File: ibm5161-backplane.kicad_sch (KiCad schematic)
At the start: 33 parts, among them J1 Bus_ISA_8bit, J2 Bus_ISA_8bit, J3 Bus_ISA_8bit, J4 Bus_ISA_8bit, J5 Bus_ISA_8bit, J6 Bus_ISA_8bit, J7 Bus_ISA_8bit, J8 Bus_ISA_8bit, P1 Molex 15-48-0106, P2 Molex 15-48-0106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

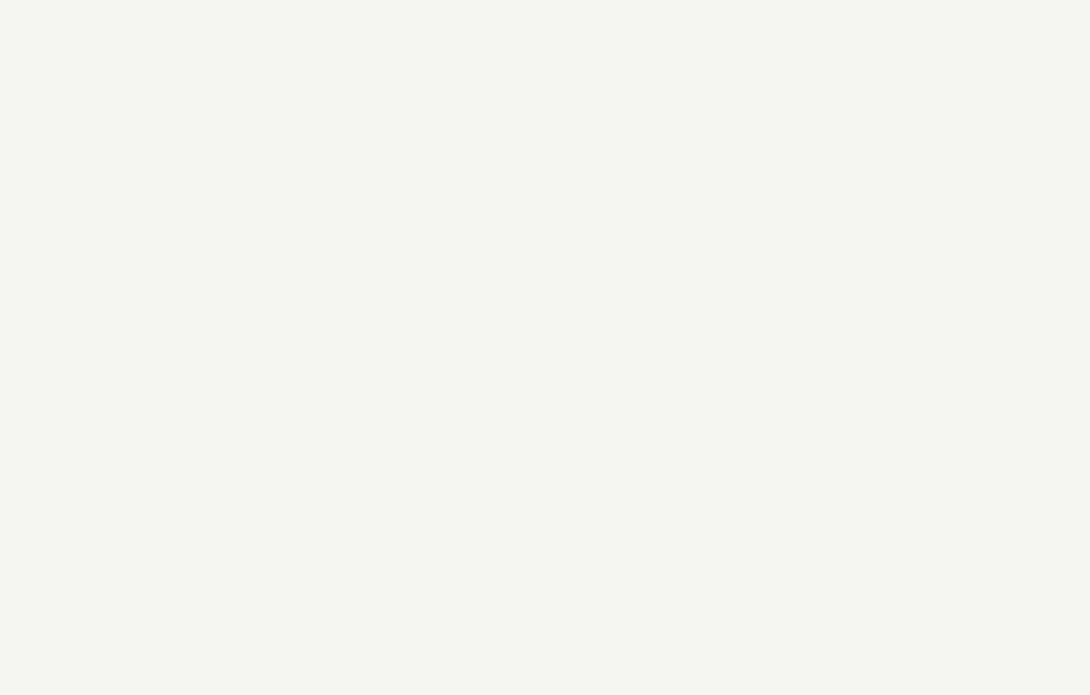
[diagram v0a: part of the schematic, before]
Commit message: Added 24 pin ATX connector and negative voltage regulator to schematic.
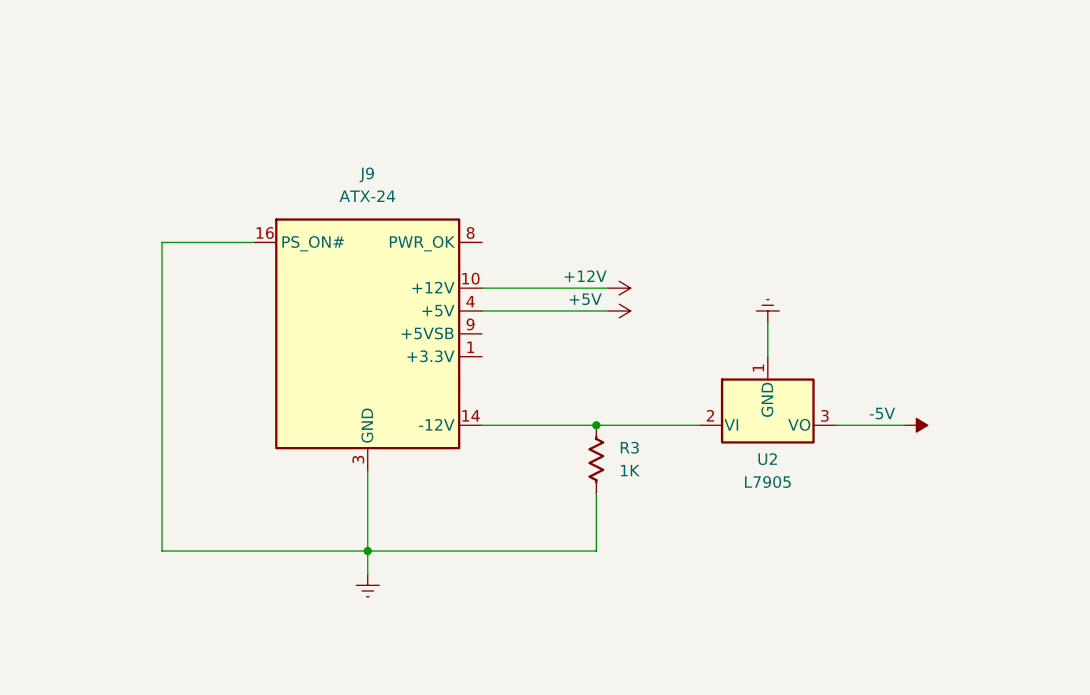
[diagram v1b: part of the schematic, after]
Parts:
- added J9: ATX-24, SamacSys_Parts:1-1775099-3, symbol Connector:ATX-24
- added R3: 1K, Library:R_Axial_DIN0207_L6.3mm_D2.5mm_P12.70mm_Horizontal, symbol Resistor_US_AKL:R_DIN0207_P10.16mm
- added U2: L7905, SamacSys_Parts:TO270P460X1020X2008-3P, symbol Regulator_Linear:L7905
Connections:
- net +12V: now also J9.10 (+12V), J9.11 (+12V)
- net +5V: now also J9.21 (+5V), J9.22 (+5V), J9.23 (+5V), J9.4 (+5V), J9.6 (+5V)
- net -5V: now also U2.3 (VO)
- net GNDREF: now also J9.15 (GND), J9.16 (PS_ON#), J9.17 (GND), J9.18 (GND), J9.19 (GND), J9.24 (GND), J9.3 (GND), J9.5 (GND), J9.7 (GND), R3.2, U2.1 (GND)
- new net: J9.1 (+3.3V), J9.12 (+3.3V), J9.13 (+3.3V), J9.2 (+3.3V)
- new net: J9.14 (-12V), R3.1, U2.2 (VI)

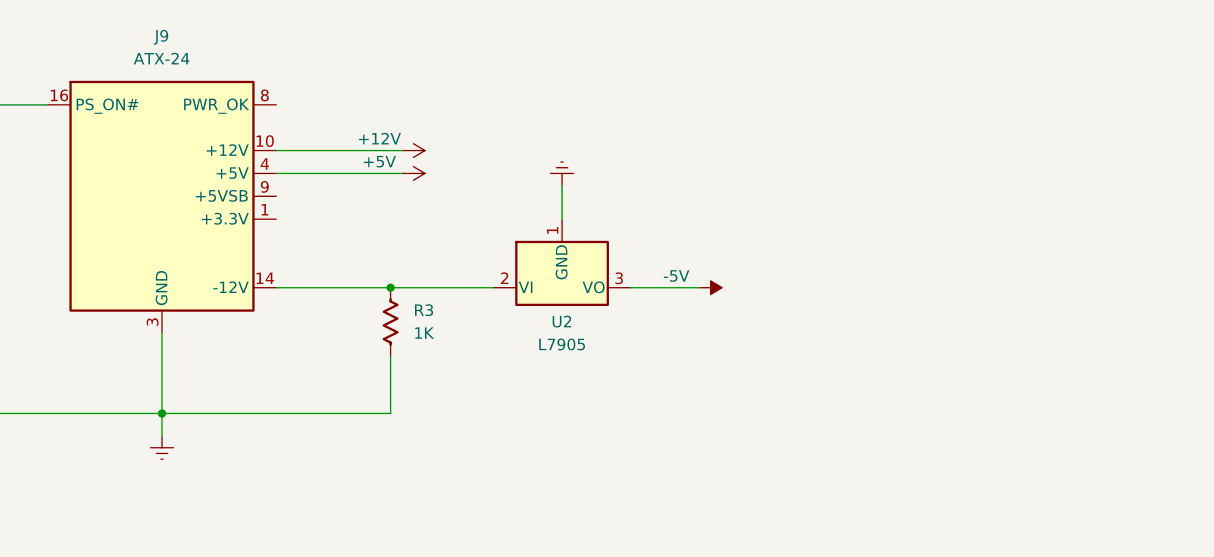
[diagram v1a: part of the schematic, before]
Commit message: Added filter caps for the L7905 and a dummy load resistor for its output
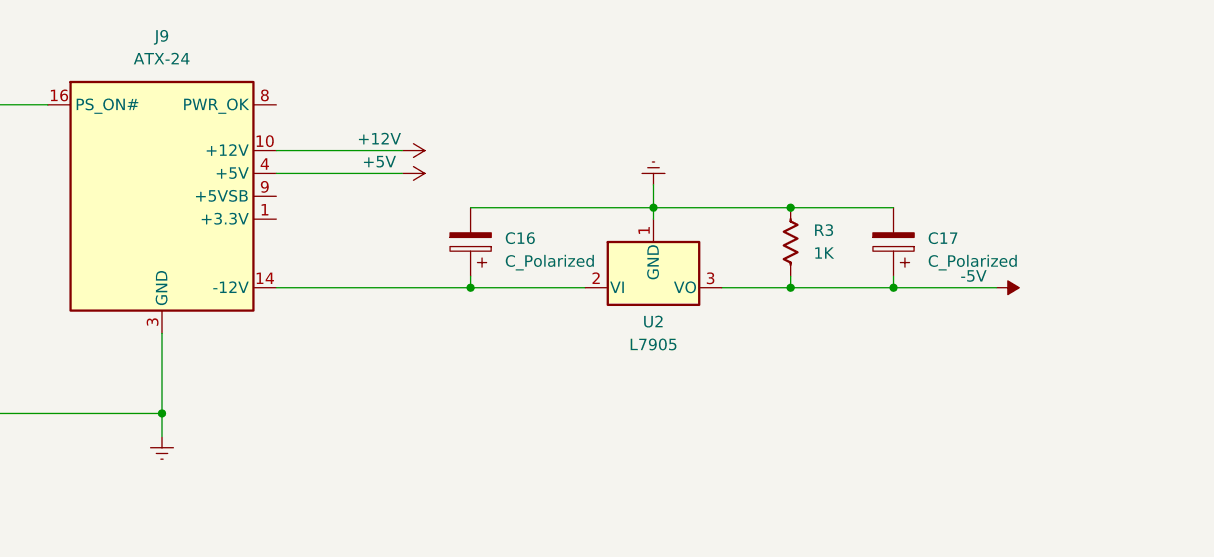
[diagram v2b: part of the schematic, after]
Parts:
- added C16, C17: C_Polarized, symbol Device:C_Polarized
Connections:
- net -5V: now also R3.2, C17.1
- net GNDREF: now also R3.1, C16.2, C17.2; no longer R3.2
- net at J9.14 (-12V), U2.2 (VI): now also C16.1; no longer R3.1
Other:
- moved on the sheet: U2

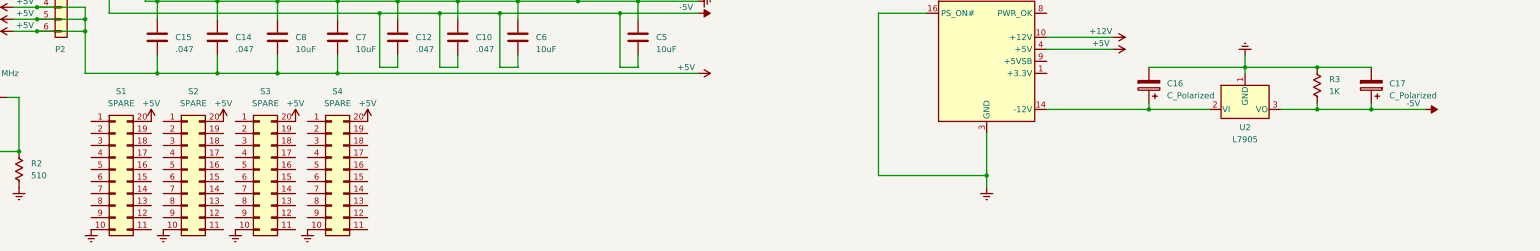
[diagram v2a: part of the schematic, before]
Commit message: Removed spare slots. Schematic cleanup.
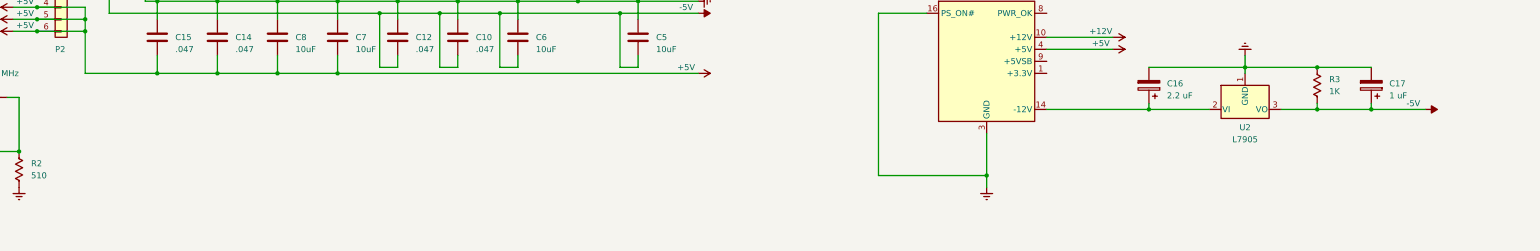
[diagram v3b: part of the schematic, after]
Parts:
- removed S1, S2, S3, S4: SPARE, Library:DIP-20_W7.62mm_Socket SQ, symbol Connector_Generic:Conn_02x10_Counter_Clockwise
- C16: value C_Polarized -> 2.2 uF; footprint (none) -> Capacitor_THT:CP_Radial_D5.0mm_P2.50mm
- C17: value C_Polarized -> 1 uF; footprint (none) -> Capacitor_THT:CP_Radial_D5.0mm_P2.50mm

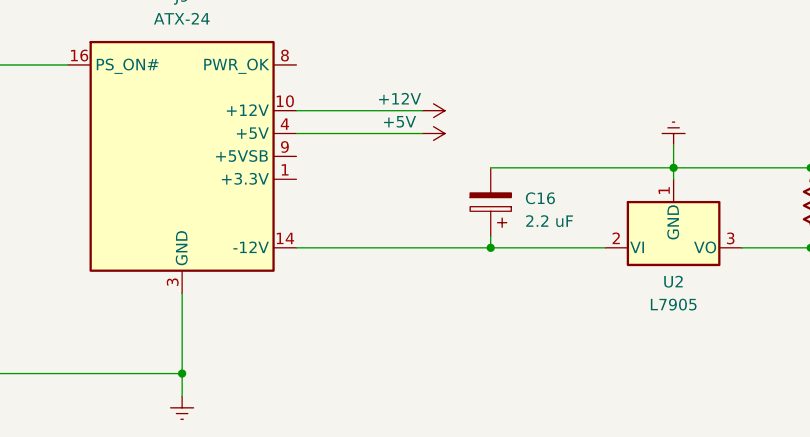
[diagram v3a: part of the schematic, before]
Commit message: Connected -12V from 24 pin to -12V rail.
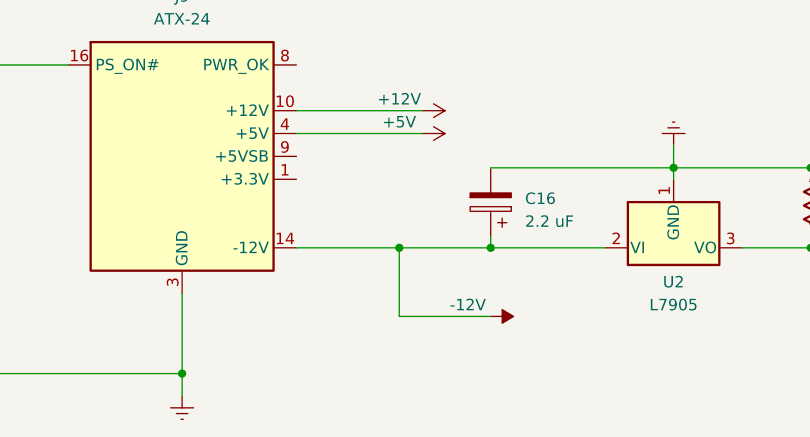
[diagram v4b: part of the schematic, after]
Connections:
- net -12V: now also C16.1, J9.14 (-12V), U2.2 (VI)
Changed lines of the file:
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@@
 	)
 	(junction
+		(at 320.04 168.91)
+		(diameter 0)
+		(color 0 0 0 0)
+	)
+	(junction
 		(at 158.75 161.29)
 		(diameter 0)
@@
 	(wire
 		(pts
+			(xy 320.04 168.91) (xy 320.04 176.53)
+		)
+		(stroke
+			(width 0)
+			(type default)
+		)
+	)
+	(wire
+		(pts
 			(xy 377.19 88.9) (xy 386.08 88.9)
 		)
@@
 	(wire
 		(pts
-			(xy 308.61 168.91) (xy 330.2 168.91)
+			(xy 308.61 168.91) (xy 320.04 168.91)
 		)
 		(stroke
@@
 		)
 	)
+	(wire
+		(pts
+			(xy 320.04 168.91) (xy 330.2 168.91)
+		)
+		(stroke
+			(width 0)
+			(type default)
+		)
+	)
 	(bus
 		(pts
@@
 	(wire
 		(pts
+			(xy 320.04 176.53) (xy 330.2 176.53)
+		)
+		(stroke
+			(width 0)
+			(type default)
+		)
+	)
+	(wire
+		(pts
 			(xy 184.15 146.05) (xy 171.45 146.05)
 		)
@@
 					(unit 1)
 				)
+			)
+		)
+	)
+	(symbol
+		(lib_id "power:-12V")
+		(at 330.2 176.53 270)
+		(mirror x)
+		(unit 1)
+		(exclude_from_sim no)
+		(in_bom yes)
+		(on_board yes)
+		(dnp no)
+		(property "Reference" "#PWR088"
+			(at 332.74 176.53 0)
+			(effects
+				(font
+					(size 1.27 1.27)
+				)
+				(hide yes)
+			)
+		)
+		(property "Value" "-12V"
+			(at 327.66 175.26 90)
+			(effects
+				(font
+					(size 1.27 1.27)
+				)
+			)
+		)
+		(property "Footprint" ""
+			(at 330.2 176.53 0)
+			(effects
+				(font
+					(size 1.27 1.27)
+				)
+				(hide yes)
+			)
+		)
+		(property "Datasheet" ""
+			(at 330.2 176.53 0)
+			(effects
+				(font
+					(size 1.27 1.27)
+				)
+				(hide yes)
+			)
+		)
+		(property "Description" ""
+			(at 330.2 176.53 0)
+			(effects
+				(font
+					(size 1.27 1.27)
+				)
+				(hide yes)
+			)
+		)
+		(pin "1"
+		)
+		(instances
+			(project "ibm5161-backplane"
+				(path "/3153ab07-b19d-413d-9c02-432affa22f92"
+					(reference "#PWR088")
+					(unit 1)
+				)

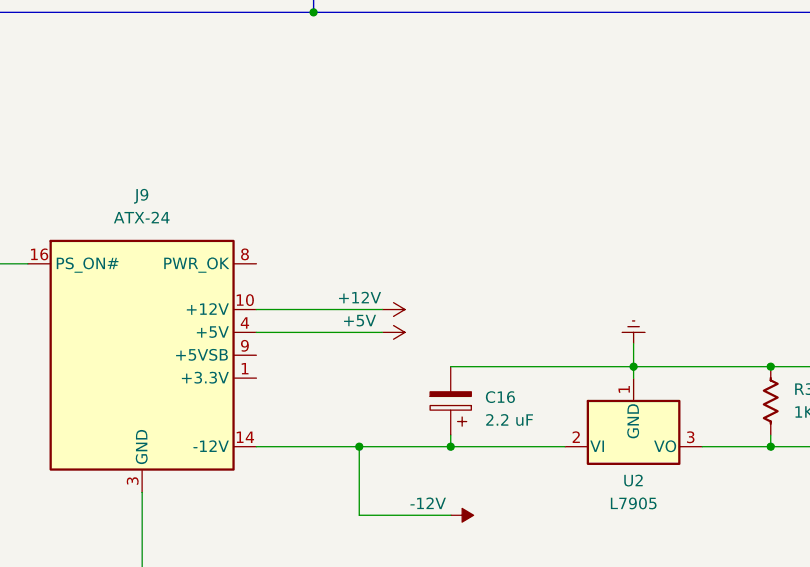
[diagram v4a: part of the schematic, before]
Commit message: Flipped 24 pin connector for easier routing. Added PWR Good LED.
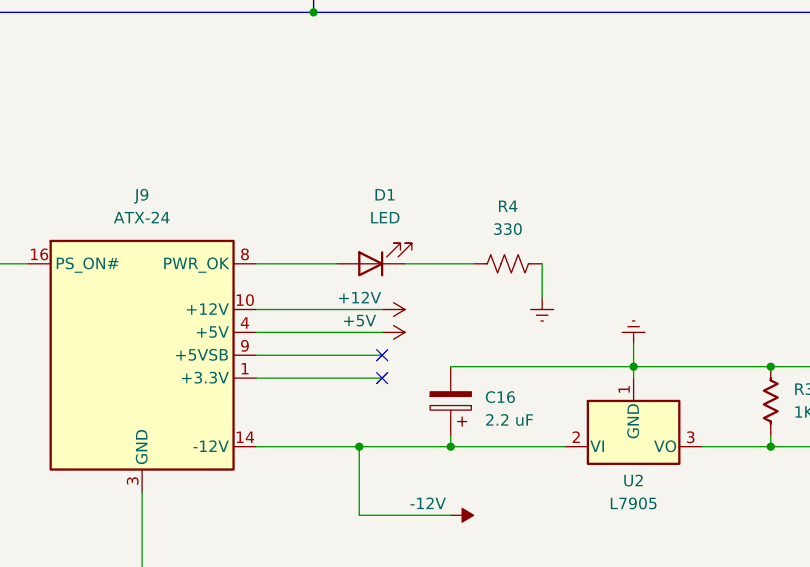
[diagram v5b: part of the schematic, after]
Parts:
- added D1: LED, LED_THT:LED_D5.0mm, symbol Device:LED
- added R4: 330, Library:R_Axial_DIN0207_L6.3mm_D2.5mm_P12.70mm_Horizontal, symbol Device:R_US
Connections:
- net GNDREF: now also R4.2
- net at J9.8 (PWR_OK): now also D1.2 (A)
- new net: D1.1 (K), R4.1
- no-connect marks 0 -> 2
